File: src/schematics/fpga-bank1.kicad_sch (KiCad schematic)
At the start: 7 parts

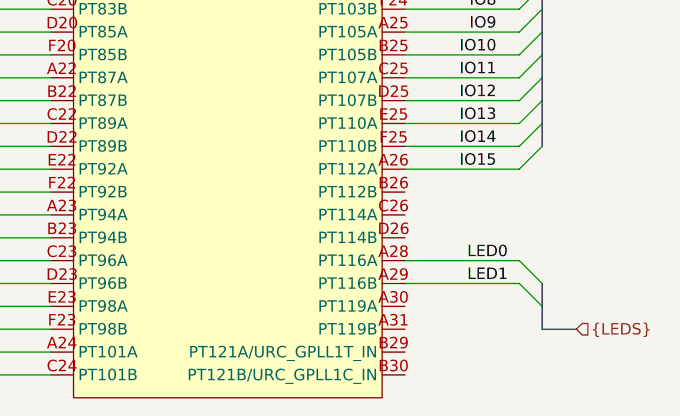
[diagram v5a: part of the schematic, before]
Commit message: Fixes bus aliases
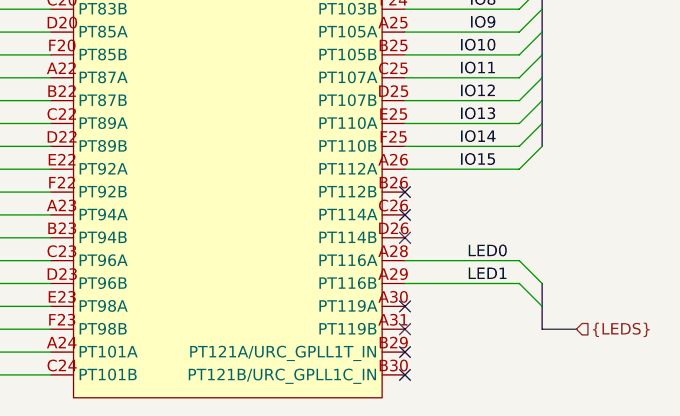
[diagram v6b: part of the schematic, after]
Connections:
- no-connect marks 0 -> 7
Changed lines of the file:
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@@
 		(color 0 0 0 0)
 	)
+	(no_connect
+		(at 172.72 146.05)
+	)
+	(no_connect
+		(at 172.72 140.97)
+	)
+	(no_connect
+		(at 172.72 125.73)
+	)
+	(no_connect
+		(at 172.72 143.51)
+	)
+	(no_connect
+		(at 172.72 130.81)
+	)
+	(no_connect
+		(at 172.72 128.27)
+	)
+	(no_connect
+		(at 172.72 138.43)
+	)
 	(bus_entry
 		(at 116.84 140.97)
@@
 		(pin "AB32"
 		)
-		(pin "AB32"
+		(pin "AB31"
 		)
 		(pin "AC26"

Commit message: Updates the root page
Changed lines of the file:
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@@
 		)
 	)
-	(hierarchical_label "{SRAM}"
+	(hierarchical_label "~{UB}"
 		(shape input)
-		(at 105.41 62.23 180)
+		(at 45.72 120.65 180)
+		(fields_autoplaced yes)
+		(effects
+			(font
+				(size 1.27 1.27)
+			)
+			(justify right)
+		)
+	)
+	(hierarchical_label "~{CE}"
+		(shape input)
+		(at 45.72 128.27 180)
 		(fields_autoplaced yes)
 		(effects
@@
 			)
 			(justify left)
+		)
+	)
+	(hierarchical_label "~{OE}"
+		(shape input)
+		(at 45.72 125.73 180)
+		(fields_autoplaced yes)
+		(effects
+			(font
+				(size 1.27 1.27)
+			)
+			(justify right)
+		)
+	)
+	(hierarchical_label "A[0..17]"
+		(shape input)
+		(at 26.67 60.96 180)
+		(fields_autoplaced yes)
+		(effects
+			(font
+				(size 1.27 1.27)
+			)
+			(justify right)
+		)
+	)
+	(hierarchical_label "IO[0..15]"
+		(shape input)
+		(at 39.37 95.25 0)
+		(fields_autoplaced yes)
+		(effects
+			(font
+				(size 1.27 1.27)
+			)
+			(justify left)
+		)
+	)
+	(hierarchical_label "~{LB}"
+		(shape input)
+		(at 45.72 118.11 180)
+		(fields_autoplaced yes)
+		(effects
+			(font
+				(size 1.27 1.27)
+			)
+			(justify right)
+		)
+	)
+	(hierarchical_label "~{WE}"
+		(shape input)
+		(at 45.72 123.19 180)
+		(fields_autoplaced yes)
+		(effects
+			(font
+				(size 1.27 1.27)
+			)
+			(justify right)
 		)
 	)
@@
 		(instances
 			(project "ecap5-bsom"
-				(path "/c5fd18a3-9aa0-4151-b6e0-94da3d606686/9ec64d27-698a-408d-bb9c-7e381193a80d/1c46737e-d838-4a0b-8b09-075a583d5a60"
+				(path "/c5fd18a3-9aa0-4151-b6e0-94da3d606686/32883292-2146-4067-bcec-7b9e760c81f8"
 					(reference "#PWR036")
 					(unit 1)
@@
 		(instances
 			(project "ecap5-bsom"
-				(path "/c5fd18a3-9aa0-4151-b6e0-94da3d606686/9ec64d27-698a-408d-bb9c-7e381193a80d/1c46737e-d838-4a0b-8b09-075a583d5a60"
+				(path "/c5fd18a3-9aa0-4151-b6e0-94da3d606686/32883292-2146-4067-bcec-7b9e760c81f8"
 					(reference "C54")
 					(unit 1)
@@
 		(instances
 			(project "ecap5-bsom"
-				(path "/c5fd18a3-9aa0-4151-b6e0-94da3d606686/9ec64d27-698a-408d-bb9c-7e381193a80d/1c46737e-d838-4a0b-8b09-075a583d5a60"
+				(path "/c5fd18a3-9aa0-4151-b6e0-94da3d606686/32883292-2146-4067-bcec-7b9e760c81f8"
 					(reference "C59")
 					(unit 1)
@@
 		(instances
 			(project "ecap5-bsom"
-				(path "/c5fd18a3-9aa0-4151-b6e0-94da3d606686/9ec64d27-698a-408d-bb9c-7e381193a80d/1c46737e-d838-4a0b-8b09-075a583d5a60"
+				(path "/c5fd18a3-9aa0-4151-b6e0-94da3d606686/32883292-2146-4067-bcec-7b9e760c81f8"
 					(reference "C56")
 					(unit 1)
@@
 		(instances
 			(project "ecap5-bsom"
-				(path "/c5fd18a3-9aa0-4151-b6e0-94da3d606686/9ec64d27-698a-408d-bb9c-7e381193a80d/1c46737e-d838-4a0b-8b09-075a583d5a60"
+				(path "/c5fd18a3-9aa0-4151-b6e0-94da3d606686/32883292-2146-4067-bcec-7b9e760c81f8"
 					(reference "C57")
 					(unit 1)
@@
 		(instances
 			(project "ecap5-bsom"
-				(path "/c5fd18a3-9aa0-4151-b6e0-94da3d606686/9ec64d27-698a-408d-bb9c-7e381193a80d/1c46737e-d838-4a0b-8b09-075a583d5a60"
+				(path "/c5fd18a3-9aa0-4151-b6e0-94da3d606686/32883292-2146-4067-bcec-7b9e760c81f8"
 					(reference "#PWR034")
 					(unit 1)
@@
 		(instances
 			(project "ecap5-bsom"
-				(path "/c5fd18a3-9aa0-4151-b6e0-94da3d606686/9ec64d27-698a-408d-bb9c-7e381193a80d/1c46737e-d838-4a0b-8b09-075a583d5a60"
+				(path "/c5fd18a3-9aa0-4151-b6e0-94da3d606686/32883292-2146-4067-bcec-7b9e760c81f8"
 					(reference "#PWR038")
 					(unit 1)
@@
 		(instances
 			(project "ecap5-bsom"
-				(path "/c5fd18a3-9aa0-4151-b6e0-94da3d606686/9ec64d27-698a-408d-bb9c-7e381193a80d/1c46737e-d838-4a0b-8b09-075a583d5a60"
+				(path "/c5fd18a3-9aa0-4151-b6e0-94da3d606686/32883292-2146-4067-bcec-7b9e760c81f8"
 					(reference "#PWR032")
 					(unit 1)
@@
 		(instances
 			(project "ecap5-bsom"
-				(path "/c5fd18a3-9aa0-4151-b6e0-94da3d606686/9ec64d27-698a-408d-bb9c-7e381193a80d/1c46737e-d838-4a0b-8b09-075a583d5a60"
+				(path "/c5fd18a3-9aa0-4151-b6e0-94da3d606686/32883292-2146-4067-bcec-7b9e760c81f8"
 					(reference "#PWR037")
 					(unit 1)
@@
 		(instances
 			(project "ecap5-bsom"
-				(path "/c5fd18a3-9aa0-4151-b6e0-94da3d606686/9ec64d27-698a-408d-bb9c-7e381193a80d/1c46737e-d838-4a0b-8b09-075a583d5a60"
+				(path "/c5fd18a3-9aa0-4151-b6e0-94da3d606686/32883292-2146-4067-bcec-7b9e760c81f8"
 					(reference "C55")
 					(unit 1)
@@
 		(instances
 			(project "ecap5-bsom"
-				(path "/c5fd18a3-9aa0-4151-b6e0-94da3d606686/9ec64d27-698a-408d-bb9c-7e381193a80d/1c46737e-d838-4a0b-8b09-075a583d5a60"
+				(path "/c5fd18a3-9aa0-4151-b6e0-94da3d606686/32883292-2146-4067-bcec-7b9e760c81f8"
 					(reference "C58")
 					(unit 1)
@@
 		(instances
 			(project "ecap5-bsom"
-				(path "/c5fd18a3-9aa0-4151-b6e0-94da3d606686/9ec64d27-698a-408d-bb9c-7e381193a80d/1c46737e-d838-4a0b-8b09-075a583d5a60"
+				(path "/c5fd18a3-9aa0-4151-b6e0-94da3d606686/32883292-2146-4067-bcec-7b9e760c81f8"
 					(reference "#PWR035")
 					(unit 1)
@@
 		(instances
 			(project "ecap5-bsom"
-				(path "/c5fd18a3-9aa0-4151-b6e0-94da3d606686/9ec64d27-698a-408d-bb9c-7e381193a80d/1c46737e-d838-4a0b-8b09-075a583d5a60"
+				(path "/c5fd18a3-9aa0-4151-b6e0-94da3d606686/32883292-2146-4067-bcec-7b9e760c81f8"
 					(reference "U6")
 					(unit 3)
@@
 		(instances
 			(project "ecap5-bsom"
-				(path "/c5fd18a3-9aa0-4151-b6e0-94da3d606686/9ec64d27-698a-408d-bb9c-7e381193a80d/1c46737e-d838-4a0b-8b09-075a583d5a60"
+				(path "/c5fd18a3-9aa0-4151-b6e0-94da3d606686/32883292-2146-4067-bcec-7b9e760c81f8"
 					(reference "#PWR033")
 					(unit 1)

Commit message: Finishes the root page
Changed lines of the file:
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@@
 		)
 	)
-	(hierarchical_label "~{UB}"
+	(hierarchical_label "SRAM.~{UB}"
 		(shape input)
 		(at 45.72 120.65 180)
@@
 		)
 	)
-	(hierarchical_label "~{CE}"
+	(hierarchical_label "SRAM.~{CE}"
 		(shape input)
 		(at 45.72 128.27 180)
@@
 		)
 	)
-	(hierarchical_label "~{OE}"
+	(hierarchical_label "SRAM.~{OE}"
 		(shape input)
 		(at 45.72 125.73 180)
@@
 		)
 	)
-	(hierarchical_label "A[0..17]"
+	(hierarchical_label "SRAM.A[0..17]"
 		(shape input)
 		(at 26.67 60.96 180)
@@
 		)
 	)
-	(hierarchical_label "IO[0..15]"
+	(hierarchical_label "SRAM.IO[0..15]"
 		(shape input)
 		(at 39.37 95.25 0)
@@
 		)
 	)
-	(hierarchical_label "~{LB}"
+	(hierarchical_label "SRAM.~{LB}"
 		(shape input)
 		(at 45.72 118.11 180)
@@
 		)
 	)
-	(hierarchical_label "~{WE}"
+	(hierarchical_label "SRAM.~{WE}"
 		(shape input)
 		(at 45.72 123.19 180)
